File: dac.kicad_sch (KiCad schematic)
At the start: 29 parts, among them U7 DAC61408RHAR

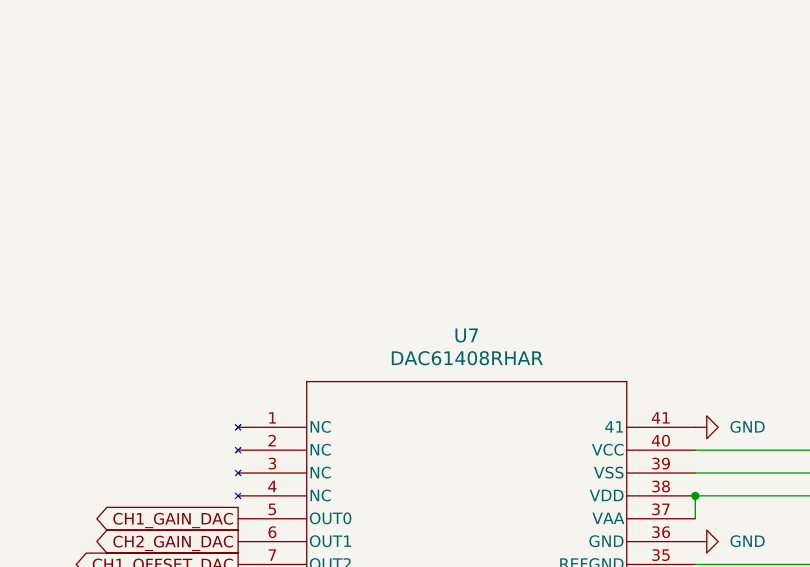
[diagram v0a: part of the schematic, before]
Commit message: Remove the stage between DAC and FET buffer
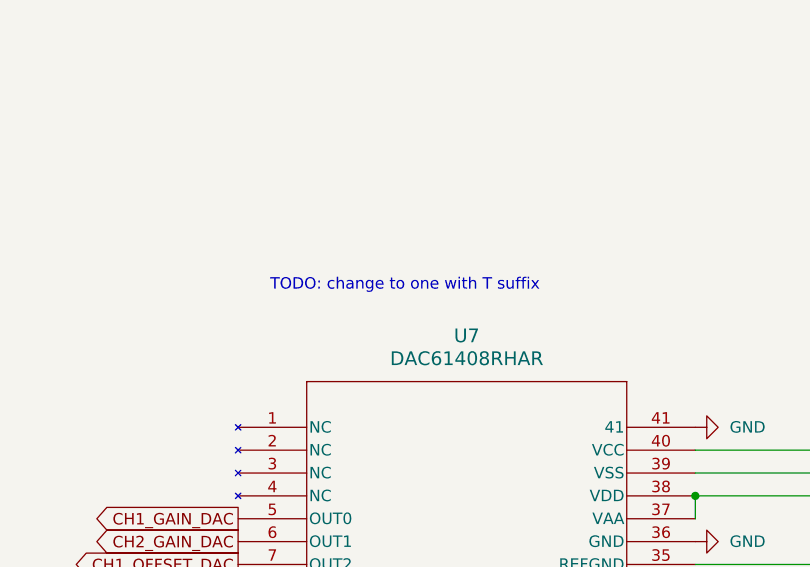
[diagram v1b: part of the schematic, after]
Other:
- note added: "TODO: change to one with T suffix"
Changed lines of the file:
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@@
 	(generator_version "9.0")
 	(paper "A3")
+	(text "TODO: change to one with T suffix"
+		(exclude_from_sim no)
+		(at 188.722 109.982 0)
+		(effects
+			(font
+				(size 1.27 1.27)
+			)
+		)
+	)
 	(junction
 		(at 292.1 78.74)

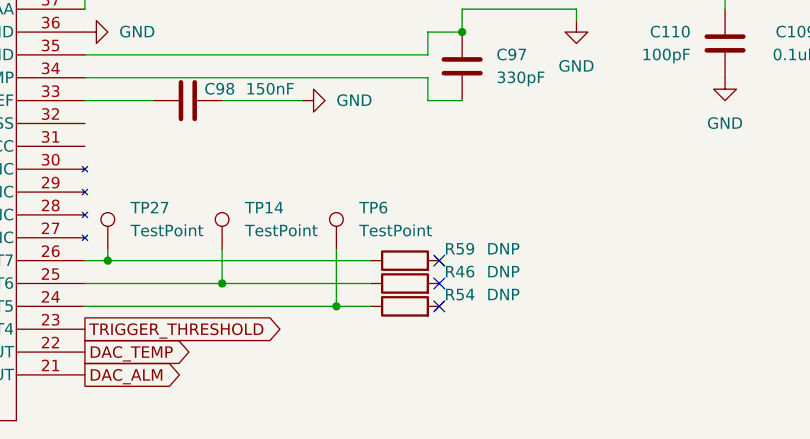
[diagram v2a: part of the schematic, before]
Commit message: Start working on ERC, properly annotate DNP elements
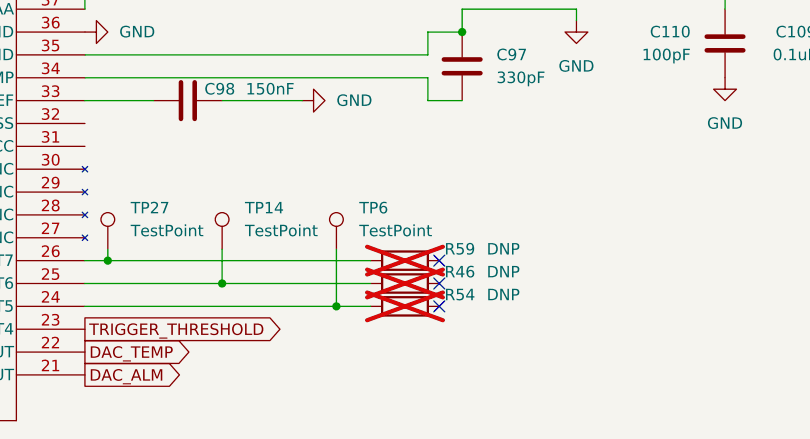
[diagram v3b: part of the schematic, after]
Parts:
- R46, R54, R59: now not fitted
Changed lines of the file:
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@@
 		(in_bom yes)
 		(on_board yes)
-		(dnp no)
+		(dnp yes)
 		(property "Reference" "R59"
 			(at 262.636 162.56 90)
@@
 		(in_bom yes)
 		(on_board yes)
-		(dnp no)
+		(dnp yes)
 		(property "Reference" "R46"
 			(at 262.636 165.1 90)
@@
 		(in_bom yes)
 		(on_board yes)
-		(dnp no)
+		(dnp yes)
 		(property "Reference" "R54"
 			(at 262.636 167.64 90)

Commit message: Fix ERC
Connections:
- net at C113.1, C114.1, C128.1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: now also U7.32 (VSS)
- net at C111.1, C112.1, C78.1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: now also U7.31 (VCC)
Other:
- moved on the sheet: C102, C109, C110, C111, C112, C113, C114, C128, C78, C97, C98, L10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

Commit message: Add all footprints
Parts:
- L51: renamed from L35; footprint (none) -> Inductor_SMD:L_0805_2012Metric
- L52: renamed from L36; footprint (none) -> Inductor_SMD:L_0805_2012Metric
- L53: renamed from L9; footprint (none) -> Inductor_SMD:L_0805_2012Metric
- L54: renamed from L43; footprint (none) -> Inductor_SMD:L_0805_2012Metric
- L55: renamed from L38; footprint (none) -> Inductor_SMD:L_0805_2012Metric
- L56: renamed from L10; footprint (none) -> Inductor_SMD:L_0805_2012Metric
- L57: renamed from L44; footprint (none) -> Inductor_SMD:L_0805_2012Metric
- L58: renamed from L37; footprint (none) -> Inductor_SMD:L_0805_2012Metric
- U17: renamed from U7; footprint (none) -> ul_DAC61408RHAR:QFN_08RHAT_TEX-L
- renumbered C99 to C126, C100 to C127, C101 to C128, C98 to C129, C97 to C130, C78 to C131, C113 to C132, C110 to C133, C111 to C134, C114 to C135, C109 to C136, C112 to C137, C128 to C138, C102 to C139, R59 to R176, R46 to R177, R54 to R178, TP27 to TP23, TP14 to TP24, TP6 to TP25
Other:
- note removed: "TODO: change to one with T suffix"

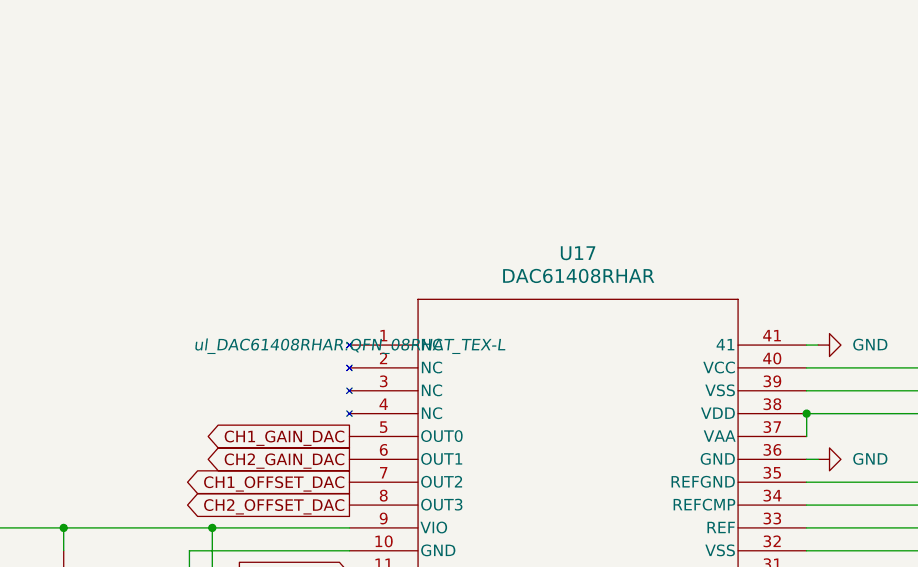
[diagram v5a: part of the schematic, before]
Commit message: Apply changes after review, left to fix: comparator histeresis, PSU missing lines?
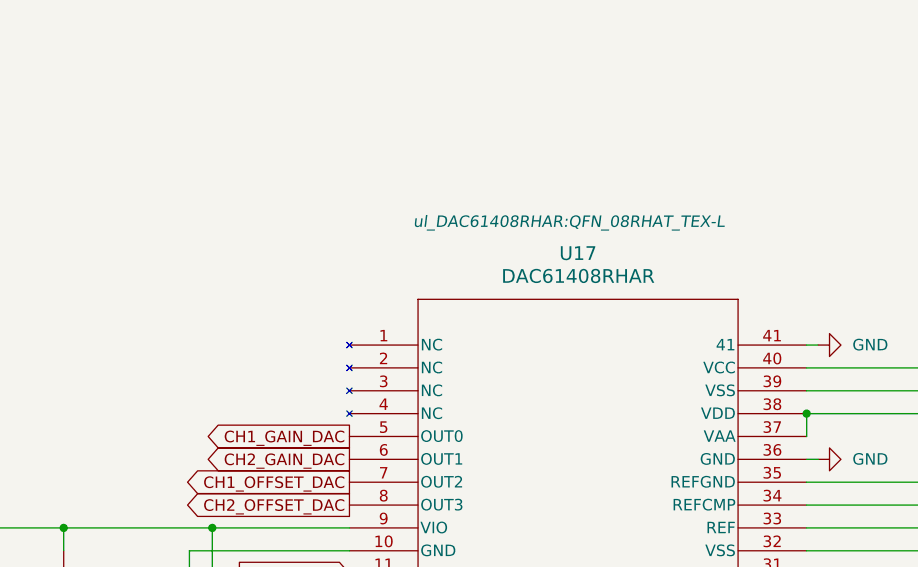
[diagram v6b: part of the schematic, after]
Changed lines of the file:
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@@
 		(on_board yes)
 		(dnp no)
-		(fields_autoplaced yes)
 		(property "Reference" "U17"
 			(at 195.58 115.57 0)
@@
 		)
 		(property "Footprint" "ul_DAC61408RHAR:QFN_08RHAT_TEX-L"
-			(at 170.18 125.73 0)
+			(at 194.564 112.014 0)
 			(effects
 				(font

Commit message: Do most of the PCB
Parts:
- removed R176, R177, R178: DNP, Resistor_SMD:R_0805_2012Metric, symbol Device:R
- added TP26: TestPoint, Connector_PinHeader_2.54mm:PinHeader_1x01_P2.54mm_Vertical, symbol Connector:TestPoint
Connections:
- net TRIGGER_THRESHOLD: no longer names the net of U17.23 (OUT4)
- net TRIGGER_THRESHOLD: now also TP26.1
- no-connect marks 3 -> 4
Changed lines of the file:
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@@
 	)
 	(junction
+		(at 261.62 171.45)
+		(diameter 0)
+		(color 0 0 0 0)
+	)
+	(junction
 		(at 238.76 128.27)
 		(diameter 0)
@@
 	)
 	(no_connect
-		(at 260.35 168.91)
+		(at 274.32 171.45)
 	)
 	(no_connect
-		(at 260.35 166.37)
+		(at 274.32 168.91)
 	)
 	(no_connect
-		(at 260.35 163.83)
+		(at 274.32 166.37)
+	)
+	(no_connect
+		(at 274.32 163.83)
 	)
 	(wire
@@
 	(wire
 		(pts
+			(xy 220.98 171.45) (xy 261.62 171.45)
+		)
+		(stroke
+			(width 0)
+			(type default)
+		)
+	)
+	(wire
+		(pts
 			(xy 331.47 133.35) (xy 331.47 135.89)
 		)
@@
 	(wire
 		(pts
-			(xy 223.52 163.83) (xy 252.73 163.83)
+			(xy 223.52 163.83) (xy 274.32 163.83)
 		)
 		(stroke
@@
 	(wire
 		(pts
+			(xy 261.62 162.56) (xy 261.62 171.45)
+		)
+		(stroke
+			(width 0)
+			(type default)
+		)
+	)
+	(wire
+		(pts
 			(xy 284.48 146.05) (xy 288.29 146.05)
 		)
@@
 	(wire
 		(pts
-			(xy 236.22 166.37) (xy 252.73 166.37)
+			(xy 236.22 166.37) (xy 274.32 166.37)
 		)
 		(stroke
@@
 	(wire
 		(pts
-			(xy 248.92 168.91) (xy 252.73 168.91)
+			(xy 248.92 168.91) (xy 274.32 168.91)
 		)
 		(stroke
@@
 	(wire
 		(pts
+			(xy 261.62 171.45) (xy 274.32 171.45)
+		)
+		(stroke
+			(width 0)
+			(type default)
+		)
+	)
+	(wire
+		(pts
 			(xy 284.48 140.97) (xy 284.48 138.43)
 		)
@@
 		)
 	)
-	(global_label "TRIGGER_THRESHOLD"
-		(shape output)
-		(at 220.98 171.45 0)
-		(fields_autoplaced yes)
-		(effects
-			(font
-				(size 1.27 1.27)
-			)
-			(justify left)
-		)
-		(property "Intersheetrefs" "${INTERSHEET_REFS}"
-			(at 243.6199 171.45 0)
-			(effects
-				(font
-					(size 1.27 1.27)
-				)
-				(justify left)
-				(hide yes)
-			)
-		)
-	)
 	(global_label "DAC_CLR"
 		(shape input)
@@
 	)
 	(symbol
-		(lib_id "Device:R")
-		(at 256.54 163.83 90)
-		(unit 1)
-		(exclude_from_sim no)
-		(in_bom yes)
-		(on_board yes)
-		(dnp yes)
-		(property "Reference" "R176"
-			(at 262.636 162.56 90)
-			(effects
-				(font
-					(size 1.27 1.27)
-				)
-			)
-		)
-		(property "Value" "DNP"
-			(at 267.462 162.56 90)
-			(effects
-				(font
-					(size 1.27 1.27)
-				)
-			)
-		)
-		(property "Footprint" "Resistor_SMD:R_0805_2012Metric"
-			(at 256.54 165.608 90)
-			(effects
-				(font
-					(size 1.27 1.27)
-				)
-				(hide yes)
-			)
-		)
-		(property "Datasheet" "~"
-			(at 256.54 163.83 0)
-			(effects
-				(font
-					(size 1.27 1.27)
-				)
-				(hide yes)
-			)
-		)
-		(property "Description" "Resistor"
-			(at 256.54 163.83 0)
-			(effects
-				(font
-					(size 1.27 1.27)
-				)
-				(hide yes)
-			)
-		)
-		(pin "1"
-		)
-		(pin "2"
-		)
-		(instances
-			(project "DigitalOsciloscope"
-				(path "/553deb7b-4100-40fe-99d2-0c7b4b56aad2/63f109b5-e3fc-444f-b815-14a9a2dd1ea3"
-					(reference "R176")
-					(unit 1)
-				)
-			)
-		)
-	)
-	(symbol
 		(lib_id "Device:C")
 		(at 257.81 146.05 90)
@@
 	)
 	(symbol
+		(lib_id "Connector:TestPoint")
+		(at 261.62 162.56 0)
+		(unit 1)
+		(exclude_from_sim no)
+		(in_bom yes)
+		(on_board yes)
+		(dnp no)
+		(property "Reference" "TP26"
+			(at 264.16 157.9879 0)
+			(effects
+				(font
+					(size 1.27 1.27)
+				)
+				(justify left)
+			)
+		)
+		(property "Value" "TestPoint"
+			(at 264.668 160.782 0)
+			(effects
+				(font
+					(size 1.27 1.27)
+				)
+				(justify left)
+			)
+		)
+		(property "Footprint" "Connector_PinHeader_2.54mm:PinHeader_1x01_P2.54mm_Vertical"
+			(at 266.7 162.56 0)
+			(effects
+				(font
+					(size 1.27 1.27)
+				)
+				(hide yes)
+			)
+		)
+		(property "Datasheet" "~"
+			(at 266.7 162.56 0)
+			(effects
+				(font
+					(size 1.27 1.27)
+				)
+				(hide yes)
+			)
+		)
+		(property "Description" "test point"
+			(at 261.62 162.56 0)
+			(effects
+				(font
+					(size 1.27 1.27)
+				)
+				(hide yes)
+			)
+		)
+		(pin "1"
+		)
+		(instances
+			(project "DigitalOsciloscope"
+				(path "/553deb7b-4100-40fe-99d2-0c7b4b56aad2/63f109b5-e3fc-444f-b815-14a9a2dd1ea3"
+					(reference "TP26")
+					(unit 1)
+				)
+			)
+		)
+	)
+	(symbol
 		(lib_id "power:GND")
 		(at 222.25 125.73 90)
@@
 	)
 	(symbol
-		(lib_id "Device:R")
-		(at 256.54 166.37 90)
-		(unit 1)
-		(exclude_from_sim no)
-		(in_bom yes)
-		(on_board yes)
-		(dnp yes)
-		(property "Reference" "R177"
-			(at 262.636 165.1 90)
-			(effects
-				(font
-					(size 1.27 1.27)
-				)
-			)
-		)
-		(property "Value" "DNP"
-			(at 267.462 165.1 90)
-			(effects
-				(font
-					(size 1.27 1.27)
-				)
-			)
-		)
-		(property "Footprint" "Resistor_SMD:R_0805_2012Metric"
-			(at 256.54 168.148 90)
-			(effects
-				(font
-					(size 1.27 1.27)
-				)
-				(hide yes)
-			)
-		)
-		(property "Datasheet" "~"
-			(at 256.54 166.37 0)
-			(effects
-				(font
-					(size 1.27 1.27)
-				)
-				(hide yes)
-			)
-		)
-		(property "Description" "Resistor"
-			(at 256.54 166.37 0)
-			(effects
-				(font
-					(size 1.27 1.27)
-				)
-				(hide yes)
-			)
-		)
-		(pin "1"
-		)
-		(pin "2"
-		)
-		(instances
-			(project "DigitalOsciloscope"
-				(path "/553deb7b-4100-40fe-99d2-0c7b4b56aad2/63f109b5-e3fc-444f-b815-14a9a2dd1ea3"
-					(reference "R177")
-					(unit 1)
-				)
-			)
-		)
-	)
-	(symbol
 		(lib_id "power:+3V3")
 		(at 68.58 142.24 0)
@@
 	)
 	(symbol
-		(lib_id "Device:R")
-		(at 256.54 168.91 90)
-		(unit 1)
-		(exclude_from_sim no)
-		(in_bom yes)
-		(on_board yes)
-		(dnp yes)
-		(property "Reference" "R178"
-			(at 262.636 167.64 90)
-			(effects
-				(font
-					(size 1.27 1.27)
-				)
-			)
-		)
-		(property "Value" "DNP"
-			(at 267.462 167.64 90)
-			(effects
-				(font
-					(size 1.27 1.27)
-				)
-			)
-		)
-		(property "Footprint" "Resistor_SMD:R_0805_2012Metric"
-			(at 256.54 170.688 90)
-			(effects
-				(font
-					(size 1.27 1.27)
-				)
-				(hide yes)
-			)
-		)
-		(property "Datasheet" "~"
-			(at 256.54 168.91 0)
-			(effects
-				(font
-					(size 1.27 1.27)
-				)
-				(hide yes)
-			)
-		)
-		(property "Description" "Resistor"
-			(at 256.54 168.91 0)
-			(effects
-				(font
-					(size 1.27 1.27)
-				)
-				(hide yes)
-			)
-		)
-		(pin "1"
-		)
-		(pin "2"
-		)
-		(instances
-			(project "DigitalOsciloscope"
-				(path "/553deb7b-4100-40fe-99d2-0c7b4b56aad2/63f109b5-e3fc-444f-b815-14a9a2dd1ea3"
-					(reference "R178")
-					(unit 1)
-				)
-			)
-		)
-	)
-	(symbol
 		(lib_id "Device:L")
 		(at 358.14 113.03 270)
@@
 		(on_board yes)
 		(dnp no)
-		(fields_autoplaced yes)
 		(property "Reference" "TP25"
 			(at 251.46 157.9879 0)
@@
 		)
 		(property "Value" "TestPoint"
-			(at 251.46 160.5279 0)
+			(at 251.714 160.782 0)
 			(effects
 				(font

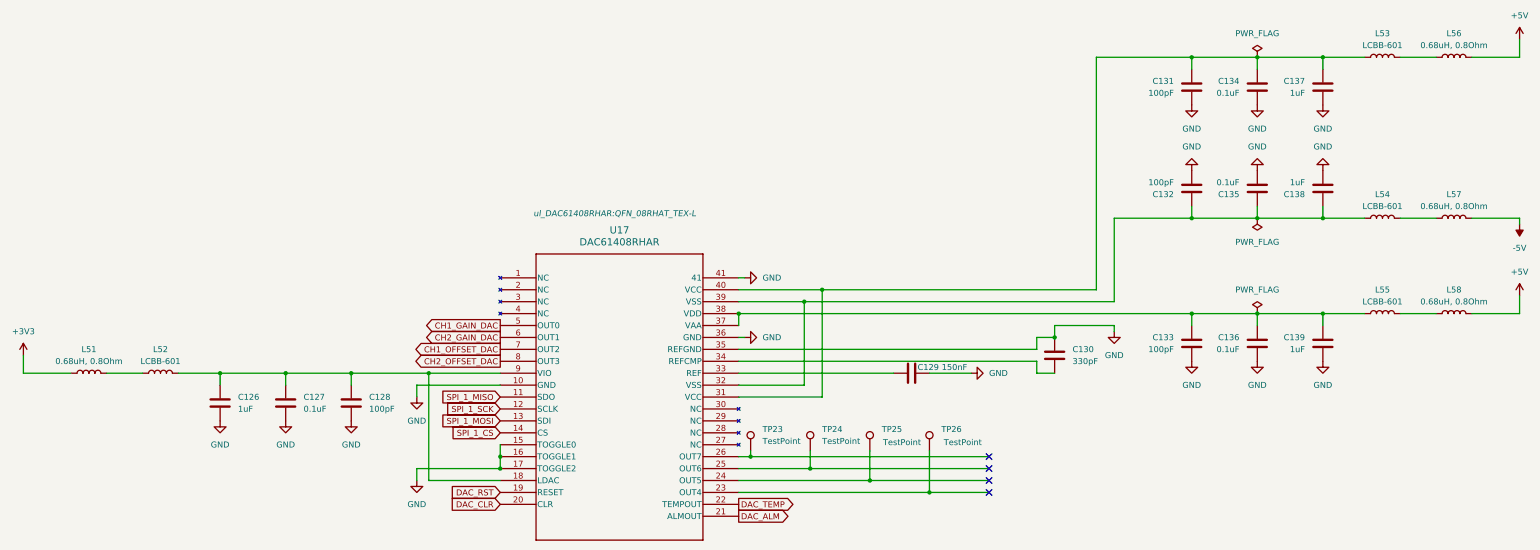
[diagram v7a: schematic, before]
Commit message: Place all componenets
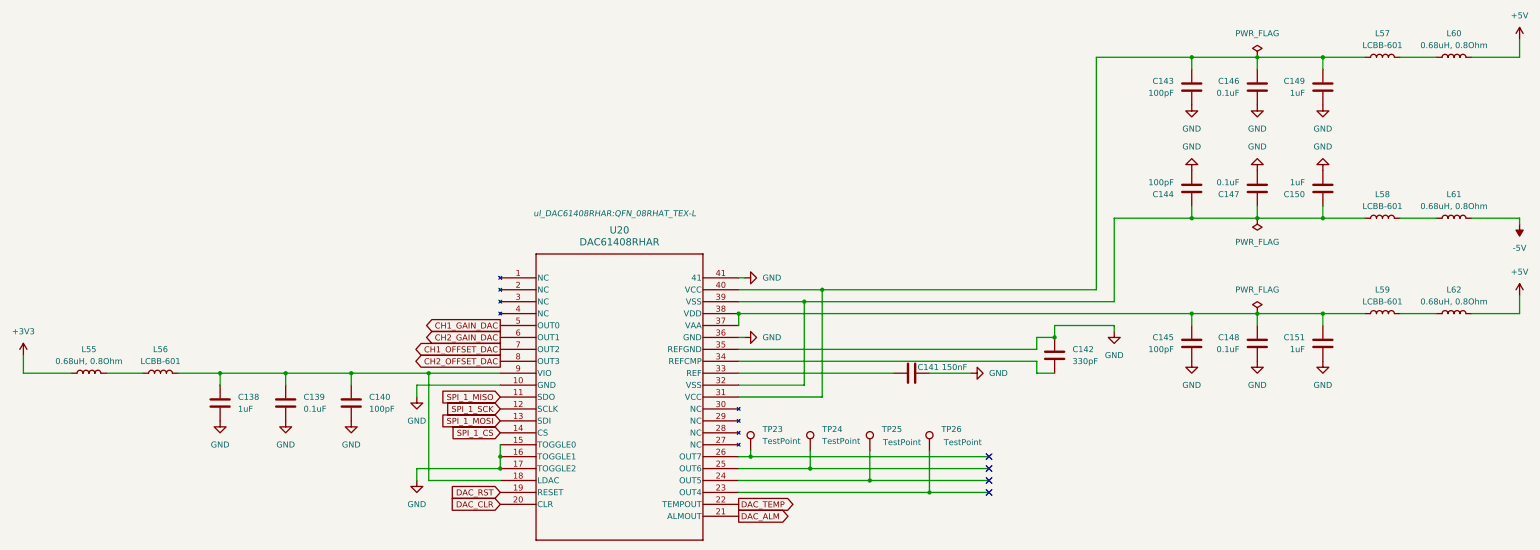
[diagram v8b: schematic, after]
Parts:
- renumbered C126 to C138, C127 to C139, C128 to C140, C129 to C141, C130 to C142, C131 to C143, C132 to C144, C133 to C145, C134 to C146, C135 to C147, C136 to C148, C137 to C149, C138 to C150, C139 to C151, L51 to L55, L52 to L56, L53 to L57, L54 to L58, L55 to L59, L56 to L60, L57 to L61, L58 to L62, U17 to U20
